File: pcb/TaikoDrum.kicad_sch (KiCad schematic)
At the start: 8 parts, among them J1 USB_B_Micro, U1 STM32F103C8Tx, U2 LM3940IMPX-3.3_NOPB

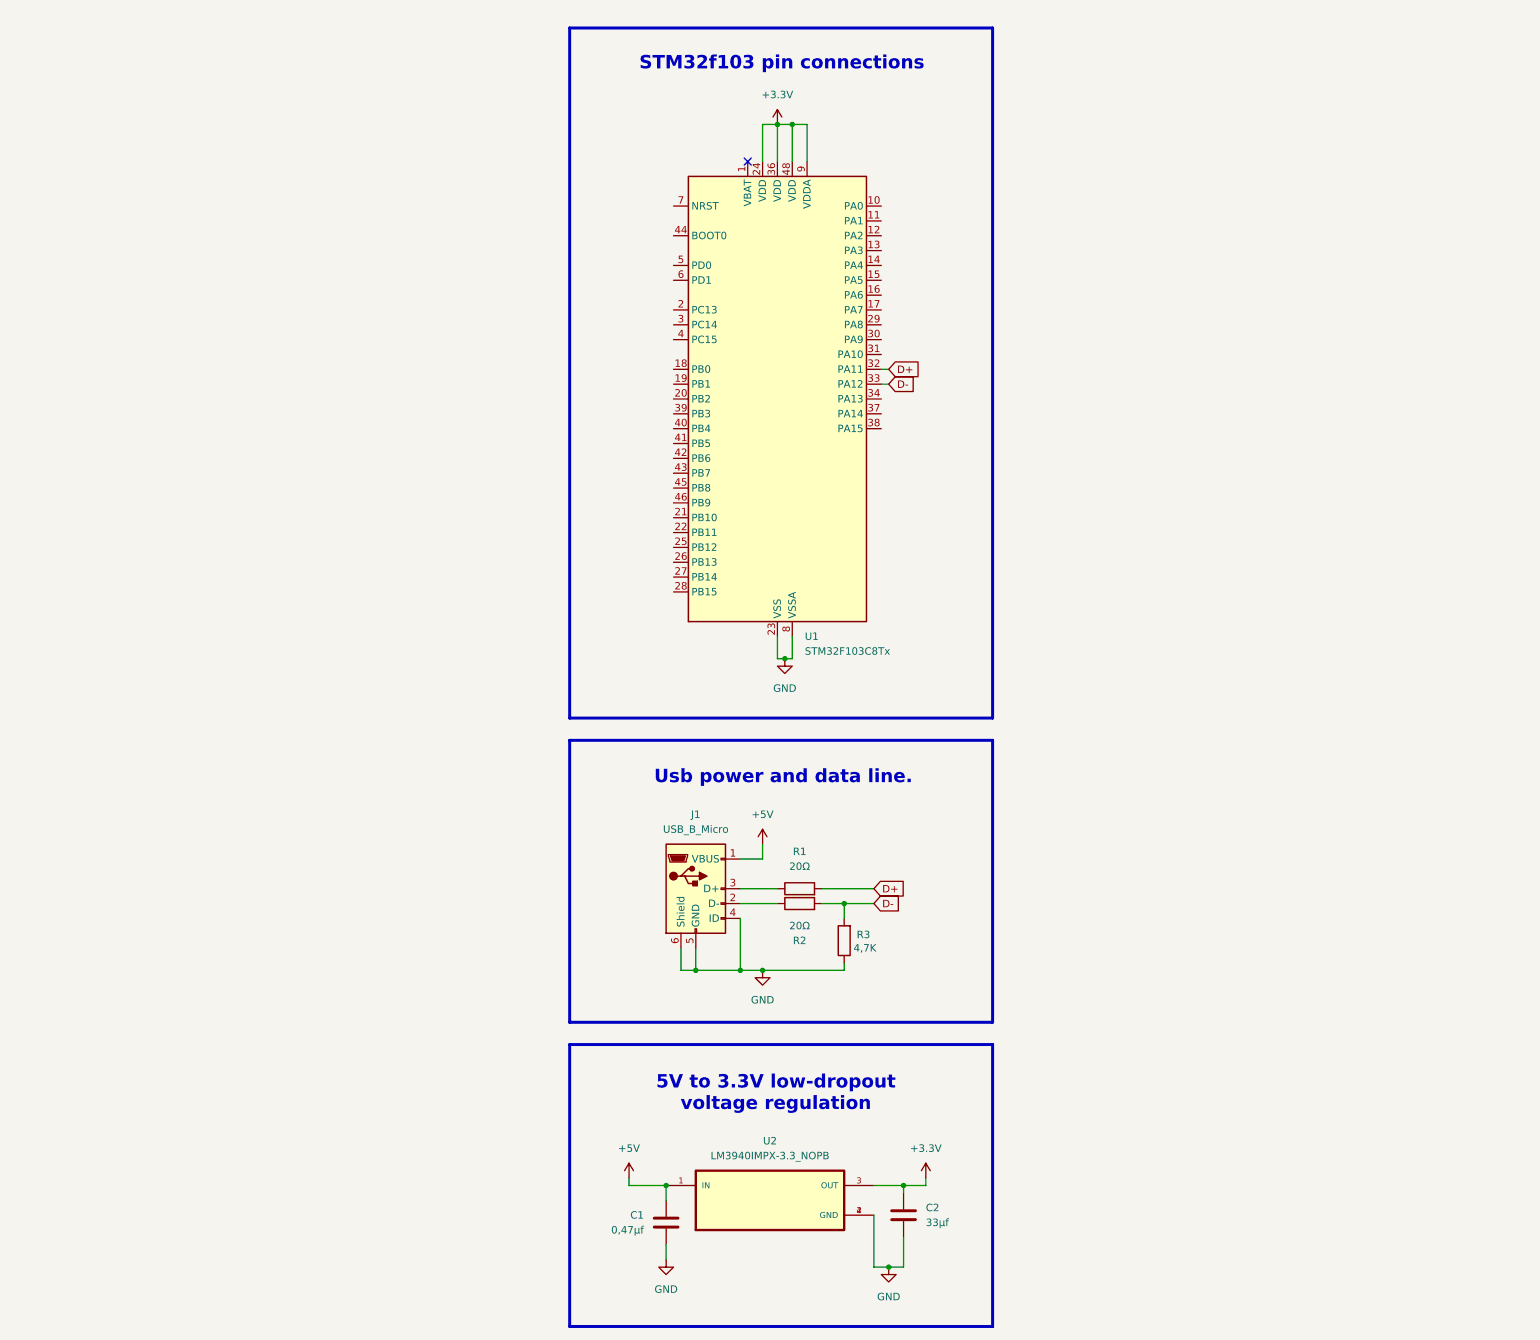
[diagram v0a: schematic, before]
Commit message: Completed the first theoretical schematic prototype.
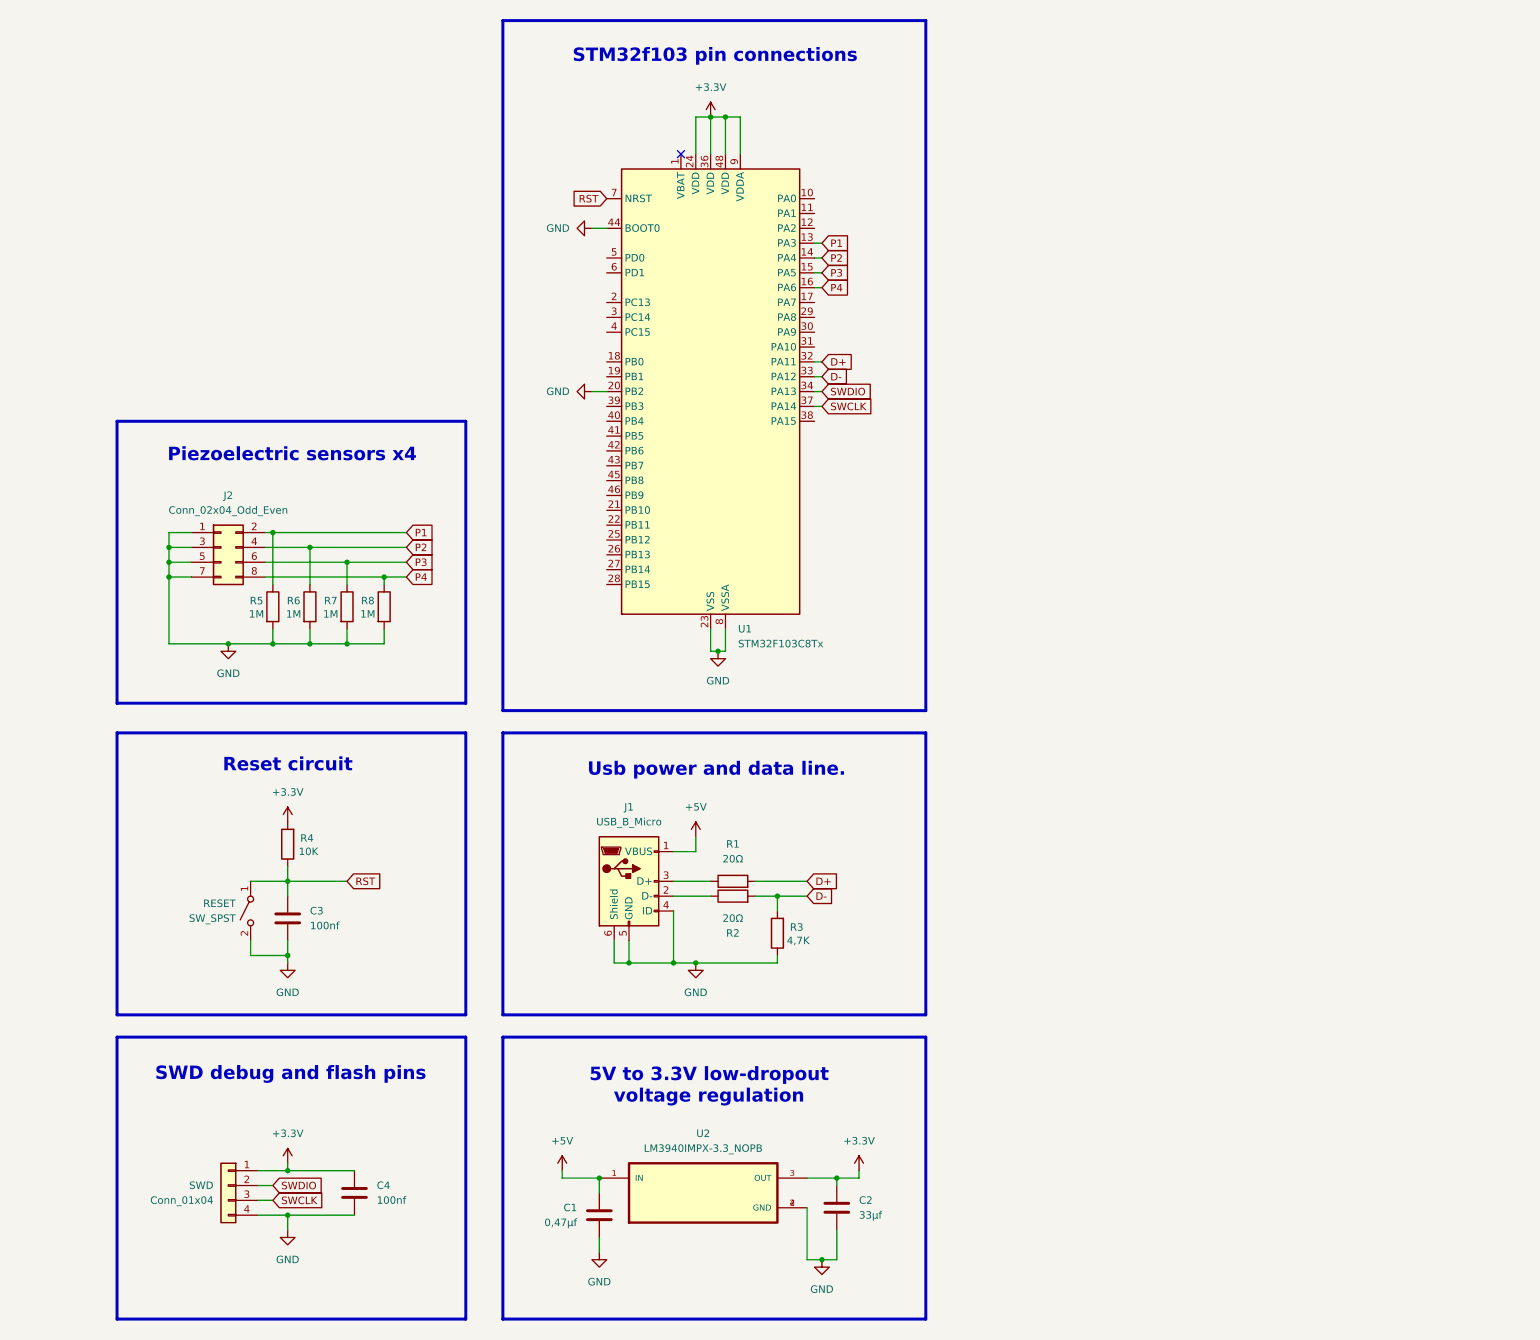
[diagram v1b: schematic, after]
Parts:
- added C3, C4: 100nf, symbol Device:C
- added J2: Conn_02x04_Odd_Even, symbol Connector_Generic:Conn_02x04_Odd_Even
- added R4: 10K, symbol Device:R
- added R5, R6, R7, R8: 1M, symbol Device:R
- added RESET: SW_SPST, symbol Switch:SW_SPST
- added SWD: Conn_01x04, symbol Connector_Generic:Conn_01x04
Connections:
- net +3.3V: now also C4.1, R4.2, SWD.1 (Pin_1)
- net GND: now also U1.20 (PB2), U1.44 (BOOT0), C3.2, C4.2, J2.1 (Pin_1), J2.3 (Pin_3), J2.5 (Pin_5), J2.7 (Pin_7), R5.2, R6.2, R7.2, R8.2, RESET.2 (B), SWD.4 (Pin_4)
- net P1: now reaches U1.13 (PA3)
- net P1: now also J2.2 (Pin_2), R5.1
- net P2: now reaches U1.14 (PA4)
- net P2: now also J2.4 (Pin_4), R6.1
- net P3: now reaches U1.15 (PA5)
- net P3: now also J2.6 (Pin_6), R7.1
- net P4: now reaches U1.16 (PA6)
- net P4: now also J2.8 (Pin_8), R8.1
- net SWDIO: now reaches U1.34 (PA13)
- net SWDIO: now also SWD.2 (Pin_2)
- net SWCLK: now reaches U1.37 (PA14)
- net SWCLK: now also SWD.3 (Pin_3)
- net RST: now reaches U1.7 (NRST)
- net RST: now also C3.1, R4.1, RESET.1 (A)
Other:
- note added: "Piezoelectric sensors x4"
- note added: "Reset circuit"
- note added: "SWD debug and flash pins"
- moved on the sheet: C1, C2, J1, R1, R2, R3, U1, U2

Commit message: Added external oscillator and decouplers for the Taiko Drum circuit.
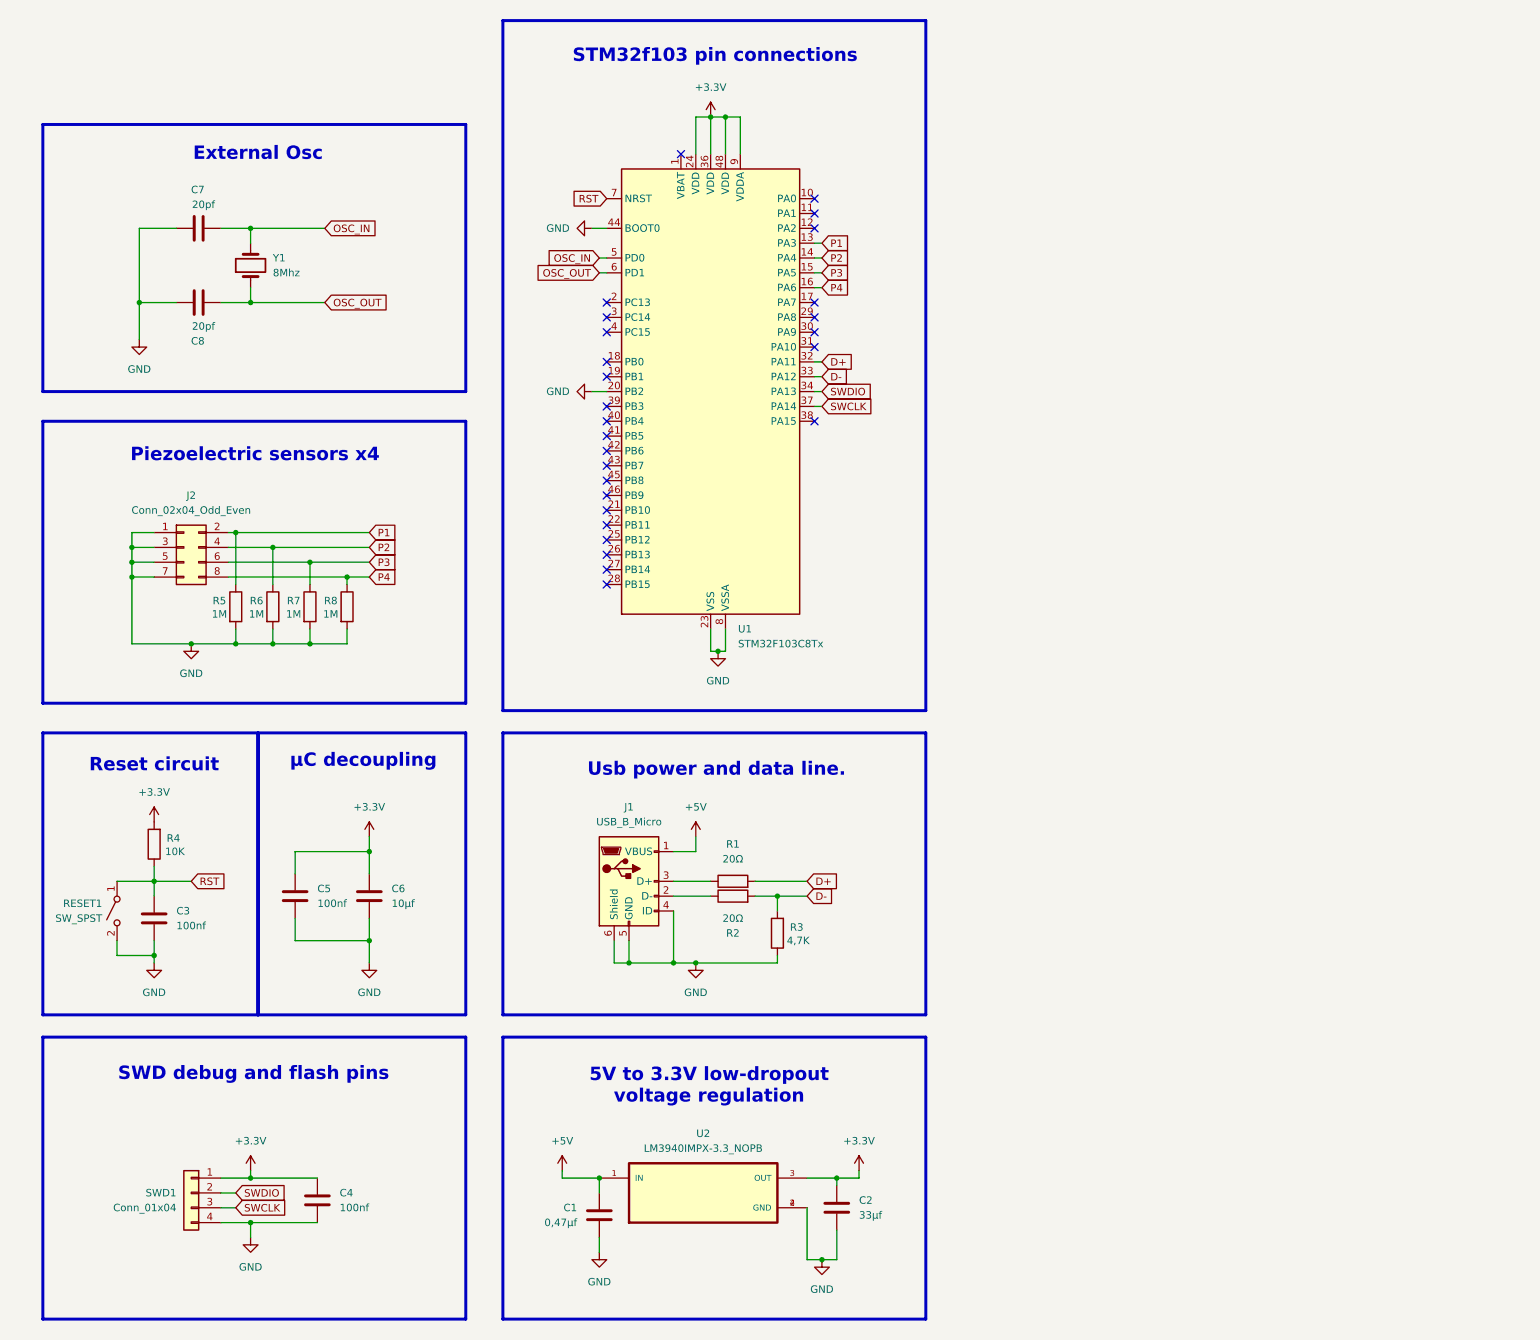
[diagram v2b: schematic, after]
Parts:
- added C5: 100nf, Capacitor_SMD:C_0805_2012Metric_Pad1.18x1.45mm_HandSolder, symbol Device:C
- added C6: 10µf, Capacitor_SMD:C_0805_2012Metric_Pad1.18x1.45mm_HandSolder, symbol Device:C
- added C7, C8: 20pf, Capacitor_SMD:C_0805_2012Metric_Pad1.18x1.45mm_HandSolder, symbol Device:C
- added Y1: 8Mhz, symbol Device:Crystal
- C1, C2, C3, C4: footprint (none) -> Capacitor_SMD:C_0805_2012Metric_Pad1.18x1.45mm_HandSolder
- J1: footprint (none) -> Connector_USB:USB_Mini-B_Wuerth_65100516121_Horizontal
- J2: footprint (none) -> Connector_PinHeader_2.54mm:PinHeader_2x04_P2.54mm_Vertical
- R1, R2, R3, R4, R5, R6, R7, R8: footprint (none) -> Resistor_SMD:R_0805_2012Metric
- SWD1: renamed from SWD; footprint (none) -> Connector_PinHeader_2.54mm:PinHeader_1x04_P2.54mm_Vertical
- renumbered RESET to RESET1
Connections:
- net +3.3V: now also C5.1, C6.1
- net GND: now also C5.2, C6.2, C7.1, C8.1
- net OSC_IN: now reaches U1.5 (PD0)
- net OSC_IN: now also C7.2, Y1.2
- net OSC_OUT: now reaches U1.6 (PD1)
- net OSC_OUT: now also C8.2, Y1.1
- no-connect marks 1 -> 27
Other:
- note added: "External Osc"
- note added: "µC decoupling"
- moved on the sheet: C3, C4, J2, R4, R5, R6, R7, R8, RESET1, SWD1
